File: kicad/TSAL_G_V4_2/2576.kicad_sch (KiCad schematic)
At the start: 3 parts, among them U18 uA7805

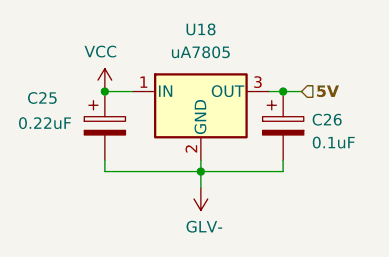
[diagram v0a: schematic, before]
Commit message: Updated TSAL G V4.2
this board already got fabbed
test is needed
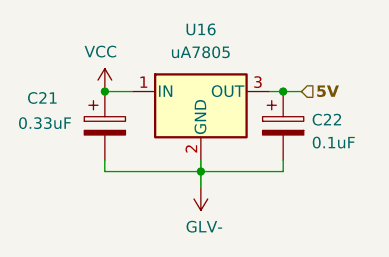
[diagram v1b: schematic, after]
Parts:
- C21: renamed from C25; value 0.22uF -> 0.33uF; footprint Better_Handsolder:CP_Radial_D10.0mm_P5.00mm_F -> Capacitor_THT:CP_Radial_D5.0mm_P2.50mm
- C22: renamed from C26; footprint Better_Handsolder:CP_Radial_D10.0mm_P5.00mm_F -> Capacitor_THT:CP_Radial_D5.0mm_P2.50mm
- renumbered U18 to U16
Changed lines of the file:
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@@
 		(on_board yes)
 		(dnp no)
-		(property "Reference" "#PWR094"
+		(property "Reference" "#PWR078"
 			(at 143.51 99.568 0)
 			(effects
@@
 			(project "TSAL_G_V4_2"
 				(path "/85dd7182-b71e-445a-95f4-dedd1af3b46e/db8961bd-328e-467f-863e-9cb426b1ad53"
-					(reference "#PWR094")
+					(reference "#PWR078")
 					(unit 1)
 				)
@@
 		(on_board yes)
 		(dnp no)
-		(property "Reference" "#PWR095"
+		(property "Reference" "#PWR079"
 			(at 154.178 102.616 0)
 			(effects
@@
 			(project "TSAL_G_V4_2"
 				(path "/85dd7182-b71e-445a-95f4-dedd1af3b46e/db8961bd-328e-467f-863e-9cb426b1ad53"
-					(reference "#PWR095")
+					(reference "#PWR079")
 					(unit 1)
 				)
@@
 		(on_board yes)
 		(dnp no)
-		(property "Reference" "U18"
+		(property "Reference" "U16"
 			(at 154.178 88.9 0)
 			(effects
@@
 			(project ""
 				(path "/85dd7182-b71e-445a-95f4-dedd1af3b46e/db8961bd-328e-467f-863e-9cb426b1ad53"
-					(reference "U18")
+					(reference "U16")
 					(unit 1)
 				)
@@
 		(on_board yes)
 		(dnp no)
-		(property "Reference" "C25"
+		(property "Reference" "C21"
 			(at 134.874 96.52 0)
 			(effects
@@
 			)
 		)
-		(property "Value" "0.22uF"
+		(property "Value" "0.33uF"
 			(at 133.858 99.314 0)
 			(effects
@@
 			)
 		)
-		(property "Footprint" "Better_Handsolder:CP_Radial_D10.0mm_P5.00mm_F"
+		(property "Footprint" "Capacitor_THT:CP_Radial_D5.0mm_P2.50mm"
 			(at 144.4752 103.378 0)
 			(effects
@@
 			(project "TSAL_G_V4_2"
 				(path "/85dd7182-b71e-445a-95f4-dedd1af3b46e/db8961bd-328e-467f-863e-9cb426b1ad53"
-					(reference "C25")
+					(reference "C21")
 					(unit 1)
 				)
@@
 		(on_board yes)
 		(dnp no)
-		(property "Reference" "C26"
+		(property "Reference" "C22"
 			(at 166.497 98.933 0)
 			(effects
@@
 			)
 		)
-		(property "Footprint" "Better_Handsolder:CP_Radial_D10.0mm_P5.00mm_F"
+		(property "Footprint" "Capacitor_THT:CP_Radial_D5.0mm_P2.50mm"
 			(at 164.2872 103.378 0)
 			(effects
@@
 			(project "TSAL_G_V4_2"
 				(path "/85dd7182-b71e-445a-95f4-dedd1af3b46e/db8961bd-328e-467f-863e-9cb426b1ad53"
-					(reference "C26")
-					(unit 1)
-				)
+					(reference "C22")
+					(unit 1)
+				)
